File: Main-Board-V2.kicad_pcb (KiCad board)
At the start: 2 copper layers, 200 x 70 mm, 68 parts, among them IC1 REG1117-5, J2 776280-1, J3 776280-1, J4 1-776163-5, K1 J107F1AS123VDC.36, K2 J107F1AS123VDC.36, K3 J107F1AS123VDC.36, Q1 2N2222A, Q2 2N2222A, Q3 2N2222A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

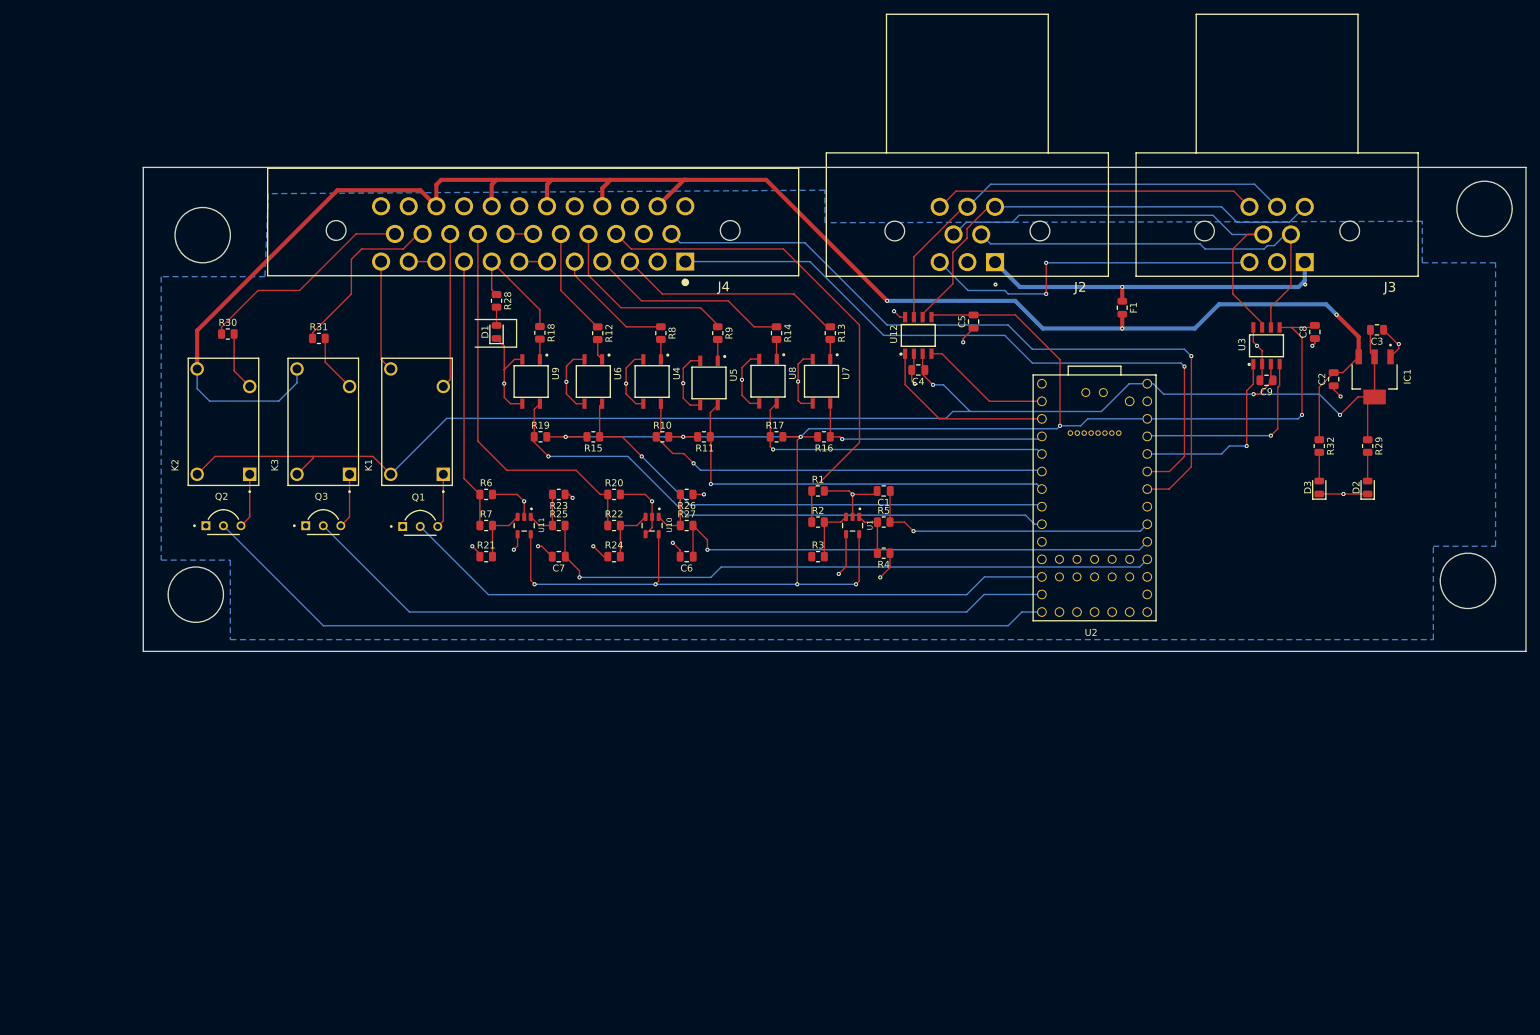
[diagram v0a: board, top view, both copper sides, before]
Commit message: fixed pcb excpet relays
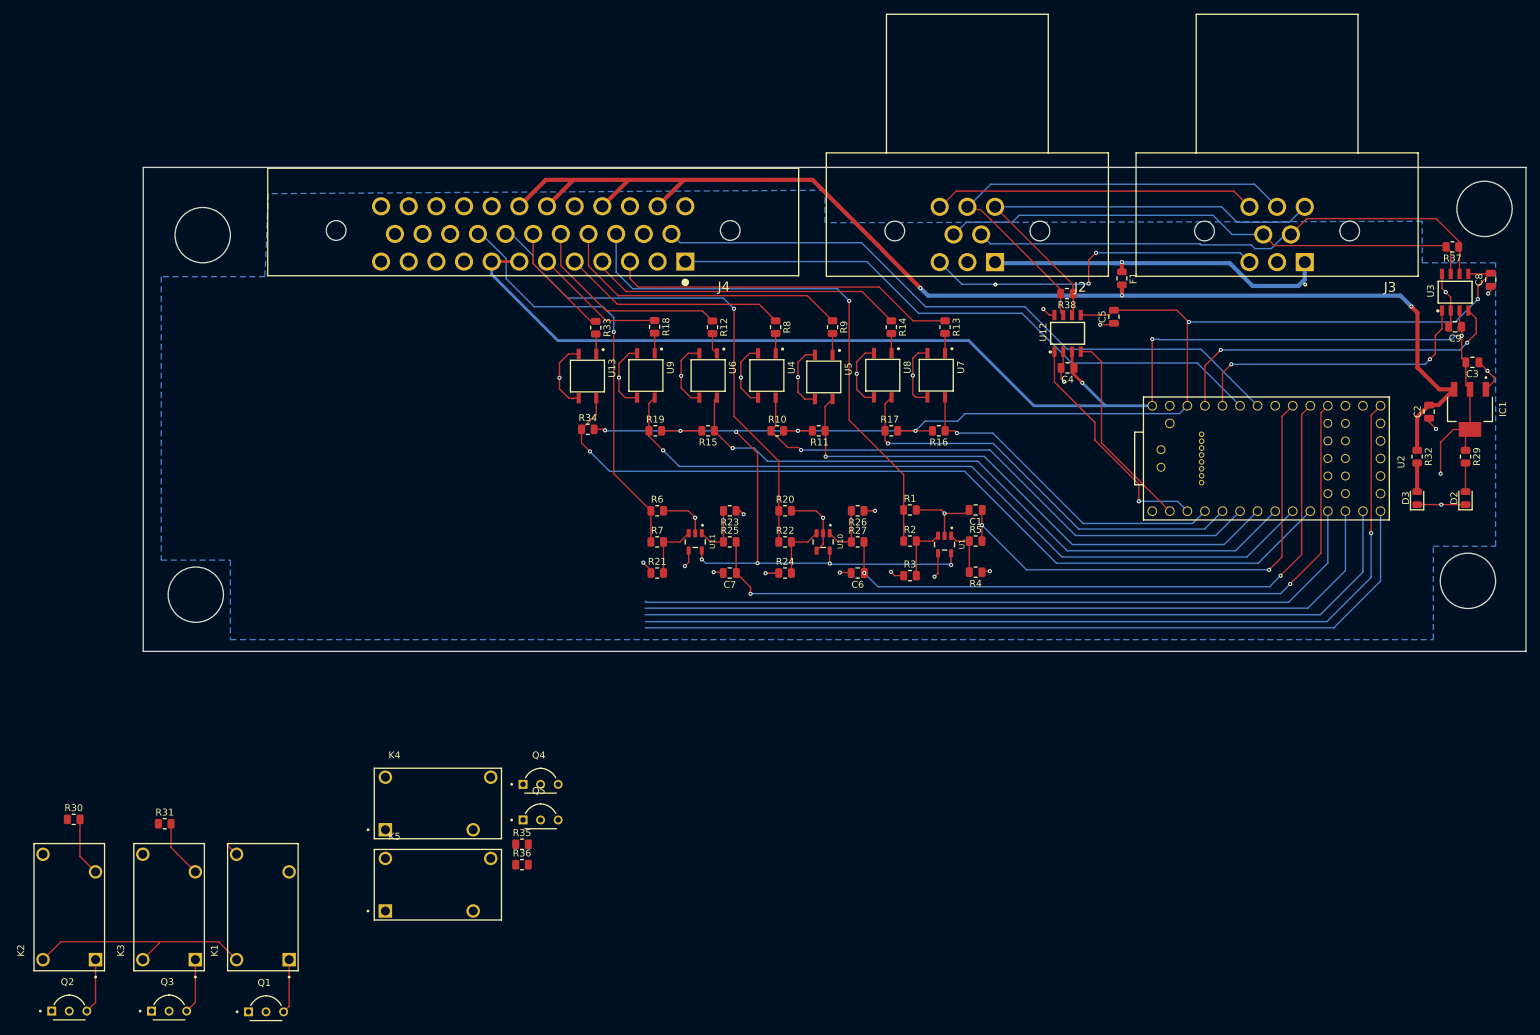
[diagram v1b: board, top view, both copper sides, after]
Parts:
- removed D1: LED, LED_SMD:LED_0805_2012Metric
- removed R28: R_US, Resistor_SMD:R_0805_2012Metric
- added K4: J107F1AS123VDC.36, PRE29-5V-S-450-1A-E:RELAY_PRE29-5V-S-450-1A-E, F.Cu at (88.5, 153.2)
- added K5: J107F1AS123VDC.36, PRE29-5V-S-450-1A-E:RELAY_PRE29-5V-S-450-1A-E, F.Cu at (88.5, 164.9)
- added Q4: 2N2222A, 2N2222A:TO92254P470H750-3, F.Cu at (103.3, 148.1)
- added Q5: 2N2222A, 2N2222A:TO92254P470H750-3, F.Cu at (103.3, 153.2)
- added R33: 10K, Resistor_SMD:R_0805_2012Metric, F.Cu at (111.3, 84.4)
- added R34: 10K, Resistor_SMD:R_0805_2012Metric, F.Cu at (110.2, 99.1)
- added R35: 10K, Resistor_SMD:R_0805_2012Metric, F.Cu at (100.7, 159.1)
- added R36: 10K, Resistor_SMD:R_0805_2012Metric, F.Cu at (100.7, 162.0)
- added R37: 120R, Resistor_SMD:R_0805_2012Metric, F.Cu at (235.2, 72.7)
- added R38: 120R, Resistor_SMD:R_0805_2012Metric, F.Cu at (179.5, 79.4)
- added U13: VOM618A-3T, VOM618A-3T:SOIC254P695X242-4N, F.Cu at (110.1, 91.4)
- R29, R32: value R_US -> 150R
- moved K1 73.7 mm to (63.2, 168.2)
- moved K2 73.7 mm to (35.2, 168.2)
- moved K3 73.7 mm to (49.6, 168.2)
- moved R31 73.7 mm to (49.0, 156.1)
- moved Q2 73.7 mm to (35.2, 180.9)
- moved Q3 73.7 mm to (49.6, 180.9)
- moved Q1 73.7 mm to (63.6, 181.0)
- moved R30 73.7 mm to (35.8, 155.5)
- moved C9 28.4 mm to (235.6, 84.2)
- moved U3 28.4 mm to (235.6, 79.2)
- moved C8 26.5 mm to (240.8, 77.4)
- moved U2 25.5 mm to (208.3, 103.3), turned to 0 degrees
- moved R21 24.9 mm to (120.2, 119.8)
- moved R6 24.9 mm to (120.2, 110.8)
- moved R7 24.9 mm to (120.2, 115.3)
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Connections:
- net /ThrottleIO renamed /Throttle1IO
- C6 pad 1: /BrakeIO -> /Throttle2IO
- J4 pad 10: /BattThrotOut -> /Relays/Horn
- J4 pad 11: /BattThrotOut -> /Relays/BattIn
- J4 pad 12: /Relays/BattIn -> /Relays/BattOut
- J4 pad 18: /Radio+ -> /Pedal/Brake
- J4 pad 19: /Radio+ -> /Pedal/Throttle2
- J4 pad 20: /Pedal/Brake+ -> /Pedal/Throttle1
- J4 pad 21: /Relays/BattOut -> /Relays/BrakeLight
- J4 pad 30: GND -> +12V
- J4 pad 31: +12V -> GND
- J4 pad 33: +12V -> GND
- J4 pad 6: /Radio- -> /PedErr
- J4 pad 7: /Radio- -> +5V
- J4 pad 8: /Pedal/Error -> +5V
- J4 pad 9: /Pedal/Throttle+ -> GND
- Q2 pad 2: /LeftSignalIO -> /RightSignalIO
- Q3 pad 2: /RightSignalIO -> /LeftSignalIO
- R18 pad 1: /Pedal/Error -> /PedErr
- R20 pad 1: /Pedal/Brake+ -> /Pedal/Throttle2
- R22 pad 1: /Pedal/Brake+ -> /Pedal/Throttle2
- R27 pad 2: /BrakeIO -> /Throttle2IO
- R6 pad 1: /Pedal/Throttle+ -> /Pedal/Throttle1
- R7 pad 1: /Pedal/Throttle+ -> /Pedal/Throttle1
- U2 pad 10: unconnected-(U2-8_TX2_IN1-Pad10) -> /BrakeIO
- U2 pad 11: unconnected-(U2-9_OUT1C-Pad11) -> /BrakeRelay
- U2 pad 20: unconnected-(U2-13_SCK_CRX1_LED-Pad20) -> /HornRelayIO
- U2 pad 24: /BrakeIO -> /Throttle2IO
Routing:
- net /HornRelayIO: track 0.00 -> 133.0 mm, vias 0 -> 1
- net /BrakeRelay: track 0.00 -> 108.8 mm
- net /Throttle2IO: track 0.00 -> 92.6 mm, vias 0 -> 2
- net +12V: track 258.2 -> 183.6 mm
- net /Pedal/Throttle2: track 0.00 -> 74.6 mm, vias 0 -> 1
- net /Pedal/Throttle1: track 0.00 -> 61.0 mm, vias 0 -> 1
- net /Pedal/Brake+: track 56.5 -> 0.00 mm
- net /BrakeIO: track 73.0 -> 123.1 mm
- net /Pedal/Throttle+: track 39.1 -> 0.00 mm
- net /Relays/RightSignal: track 31.7 -> 0.00 mm
- net /EncoderIO: track 42.7 -> 73.9 mm, vias 1 -> 2
- net /Relays/LeftSignal: track 25.6 -> 0.00 mm
- net /ErrorIO: track 84.3 -> 109.0 mm
- net /Throttle1IO: track 91.6 -> 115.0 mm, vias 1 -> 2
- net /Dio5: track 73.1 -> 95.6 mm
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
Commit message: complete. Minor Tweaks
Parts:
- moved R36 77.5 mm to (97.8, 84.6)
- moved K1 75.6 mm to (83.6, 95.4)
- moved K3 75.6 mm to (70.0, 95.4)
- moved K2 75.6 mm to (55.6, 95.4)
- moved Q3 75.6 mm to (70.0, 108.1)
- moved R31 75.6 mm to (69.4, 83.3)
- moved Q1 75.6 mm to (84.0, 108.2)
- moved Q2 75.6 mm to (55.6, 108.1)
- moved R30 75.6 mm to (56.2, 82.7)
- moved K5 69.9 mm to (98.2, 95.7), turned to 90 degrees
- moved R35 56.1 mm to (62.4, 118.0), turned to -90 degrees
- moved Q5 45.2 mm to (99.1, 108.2)
- moved K4 33.5 mm to (75.6, 122.3), turned to 180 degrees
- moved Q4 28.3 mm to (87.7, 124.5), turned to 90 degrees
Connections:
- K1 pad 3: /Relays/BattOut -> /Relays/BattIn
- K1 pad 4: /Relays/BattIn -> /Relays/BattOut
- R30 pad 1: /Relays/RightSignal -> /Relays/LeftSignal
- R31 pad 1: /Relays/LeftSignal -> /Relays/BrakeLight
- R35 pad 1: /Relays/BrakeLight -> /Relays/RightSignal
- U2 pad 11: /BrakeRelay -> /HornIO
- U2 pad 13: /RightSignalIO -> /LeftSignalIO
- U2 pad 14: /LeftSignalIO -> /RightSignalIO
- U2 pad 20: /HornRelayIO -> /BrakeRelay
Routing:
- net +12V: track 183.6 -> 340.1 mm, vias 3 -> 4
- net /HornIO: track 0.00 -> 133.6 mm
- net /HornRelayIO: track 133.0 -> 0.00 mm, vias 1 -> 0
- net /RightSignalIO: track 115.2 -> 196.0 mm
- net /Relays/RightSignal: track 0.00 -> 57.7 mm
- net +5V: track 240.2 -> 296.4 mm, vias 4 -> 3
- net /BrakeRelay: track 108.8 -> 162.5 mm, vias 0 -> 1
- net /LeftSignalIO: track 119.3 -> 170.1 mm
- net /BattRelay: track 112.2 -> 152.5 mm
- net /Relays/LeftSignal: track 0.00 -> 37.8 mm
- net /Relays/BrakeLight: track 0.00 -> 27.1 mm
- net /Relays/BattIn: track 1.98 -> 16.7 mm
- net /Relays/Horn: track 0.00 -> 13.4 mm
- net /Relays/BattOut: track 0.00 -> 12.4 mm
- net Net-(K4-Pad1): track 0.00 -> 8.33 mm
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
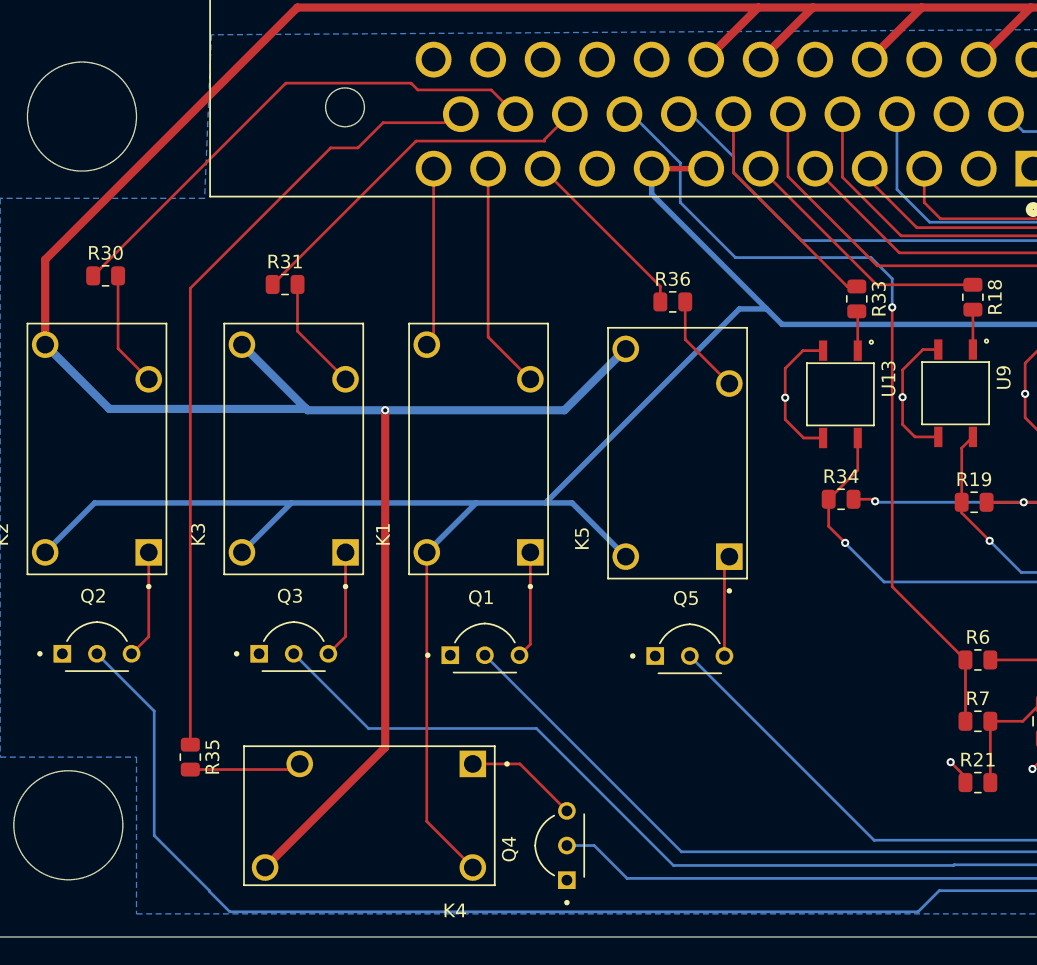
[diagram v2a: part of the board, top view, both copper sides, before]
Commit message: removed resistors for light boards
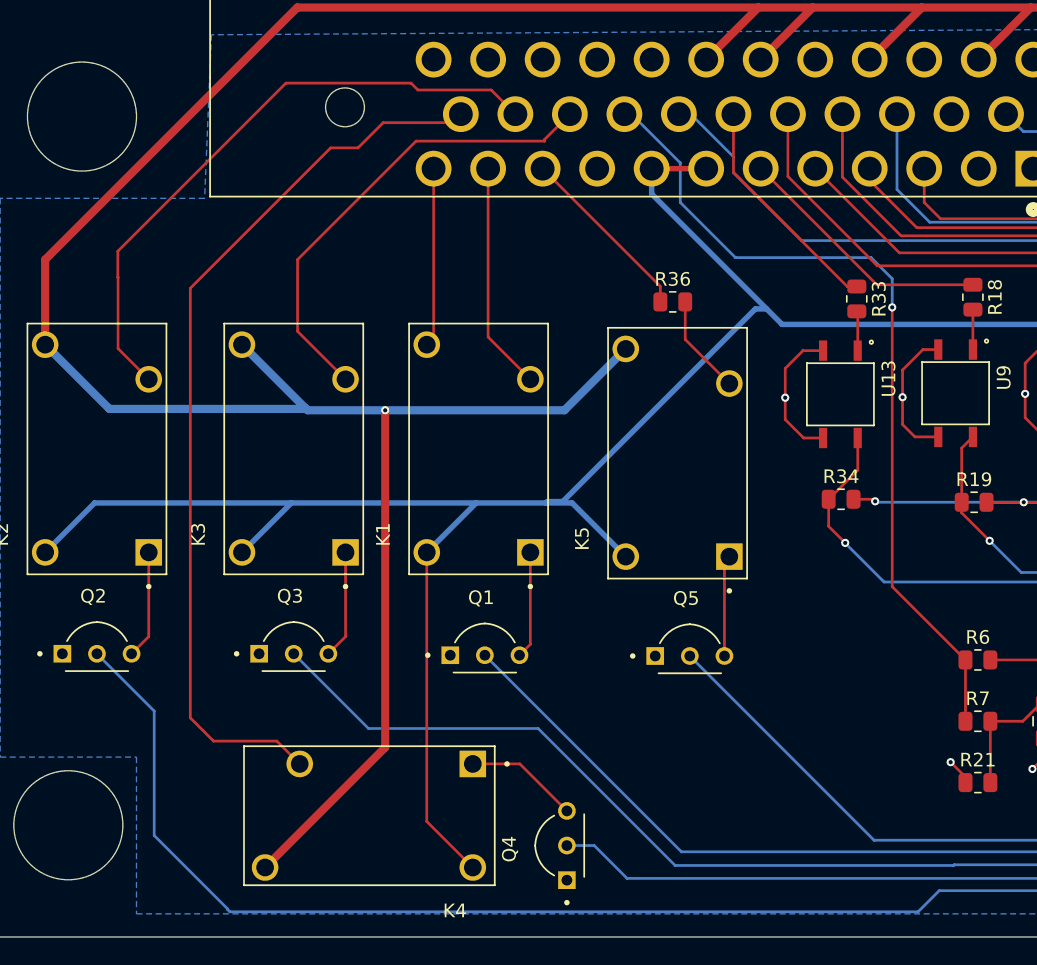
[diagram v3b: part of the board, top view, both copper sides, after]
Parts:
- removed R30, R31, R35: 10K, Resistor_SMD:R_0805_2012Metric
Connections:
- K2 pad 3: Net-(K2-Pad3) -> /Relays/LeftSignal
- K3 pad 3: Net-(K3-Pad3) -> /Relays/BrakeLight
- K4 pad 3: Net-(K4-Pad3) -> /Relays/RightSignal
- Q2 pad 2: /RightSignalIO -> /LeftSignalIO
- Q3 pad 2: /LeftSignalIO -> /BrakeRelay
- Q4 pad 2: /BrakeRelay -> /RightSignalIO
- U2 pad 13: /LeftSignalIO -> /BrakeRelay
- U2 pad 14: /RightSignalIO -> /LeftSignalIO
- U2 pad 20: /BrakeRelay -> /RightSignalIO
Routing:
- net /RightSignalIO: track 196.0 -> 162.5 mm, vias 0 -> 1
- net /LeftSignalIO: track 170.1 -> 196.0 mm
- net Net-(K2-Pad3): track 8.52 -> 0.00 mm
- net Net-(K3-Pad3): track 8.41 -> 0.00 mm
- net /Relays/LeftSignal: track 37.8 -> 45.6 mm
- net /Relays/BrakeLight: track 27.1 -> 34.7 mm
- net /BrakeRelay: track 162.5 -> 170.1 mm, vias 1 -> 0
- net Net-(K4-Pad3): track 7.61 -> 0.00 mm
- net /Relays/RightSignal: track 57.7 -> 65.2 mm
